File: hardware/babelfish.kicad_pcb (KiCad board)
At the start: 4 copper layers, 56 x 45.2 mm, 97 parts, among them J1 Shifter Power, J2 SWD, J3 DE9 Female, J4 USB_A, Q1 BSS138, SW1 TS342A2P-WZ, SW2 TS342A2P-WZ, SW3 SK12D07VG5_C3020419, U1 RP2040, U10 74HC4052PW,118, U11 MAX3232IDR, U12 AP2191WG-7, U2 TPS2113ADRBR, U3 GT-USB-7010ASV, U4 W25Q128JVS, U5 TPMCP1703T-5002E_CB, U6 TPMCP1703T-3302E_CB, U7 74HC4052PW,118, U8 74HC4052PW,118, U9 74HC4052PW,118, X1 X322512MSB4SI

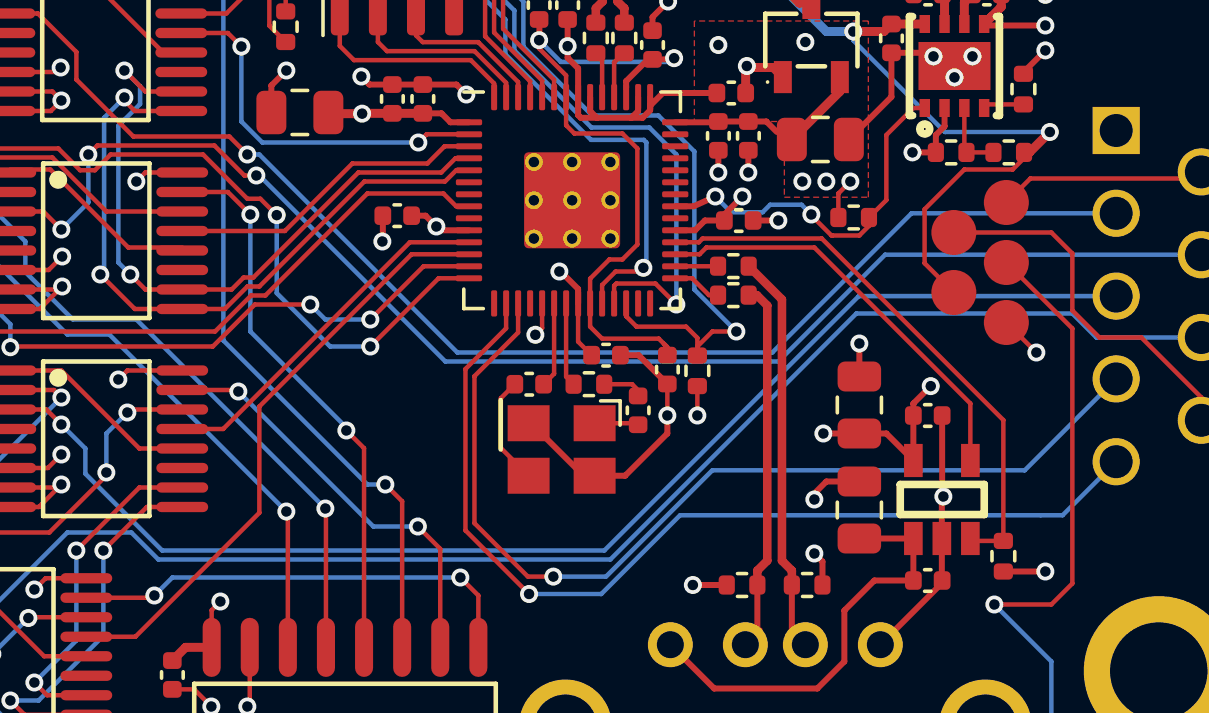
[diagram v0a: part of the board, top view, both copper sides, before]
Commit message: Er, forgot to wire CH_B_S0/1
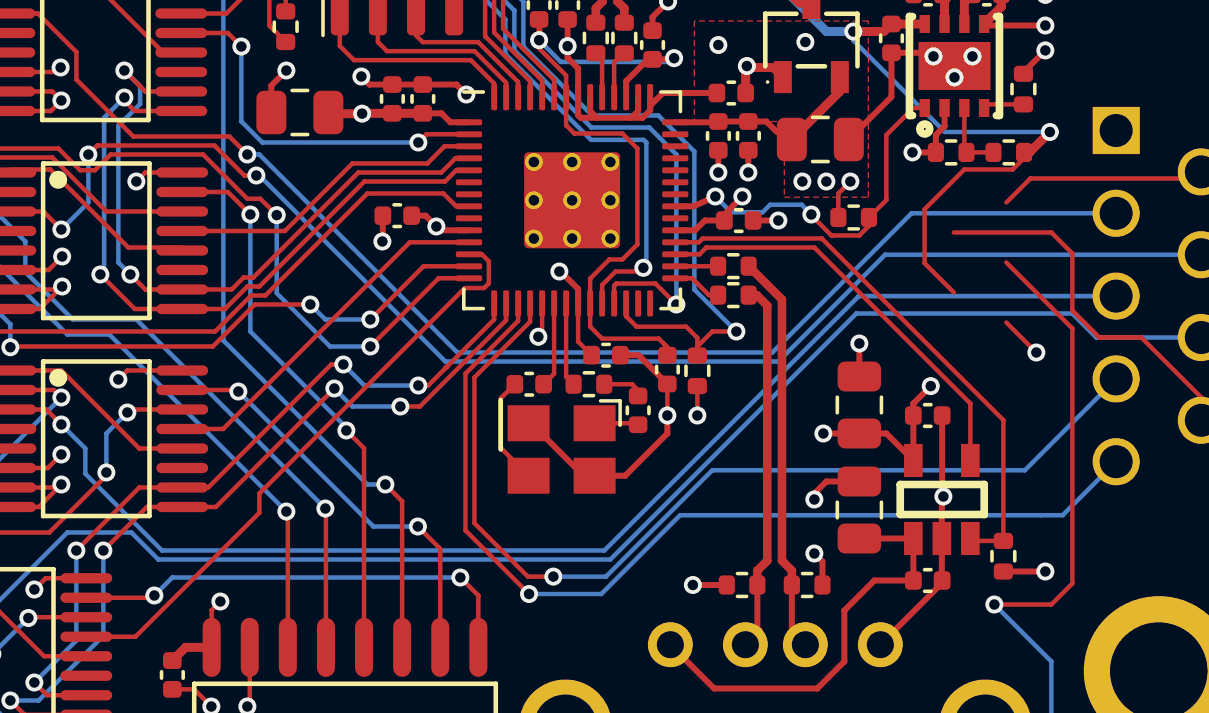
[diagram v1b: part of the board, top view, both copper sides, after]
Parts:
- removed ? (x5): , 
- D3: value Blue -> Red
- R15, R16, R17: value 68 -> 1k
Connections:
- J3 pad 4: /GPIO14 -> /GPIO15
- J3 pad 5: /GPIO13 -> /GPIO14
- U1 pad 15: /GPIO12 -> /CH_B_S0
- U1 pad 16: /GPIO13 -> /CH_B_S1
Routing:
- net /GPIO15: track 0.00 -> 33.0 mm, vias 0 -> 1
- net /GPIO13: track 32.5 -> 0.00 mm, vias 1 -> 0
- net /CH_B_S1: track 12.8 -> 27.2 mm, vias 2 -> 4
- net /CH_B_S0: track 11.3 -> 25.2 mm, vias 2 -> 4

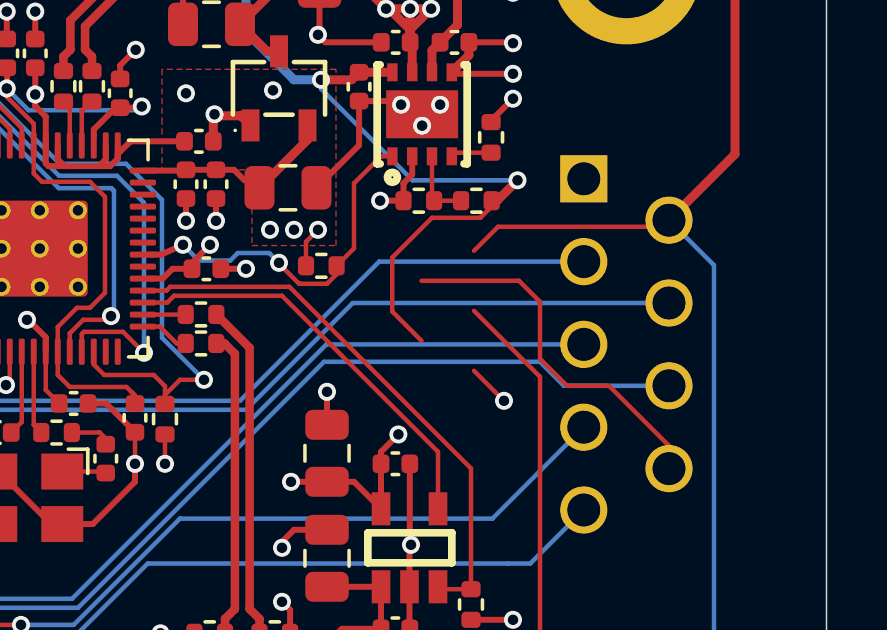
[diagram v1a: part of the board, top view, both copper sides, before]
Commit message: hw: Add back test points to schematic, fix db9 GND
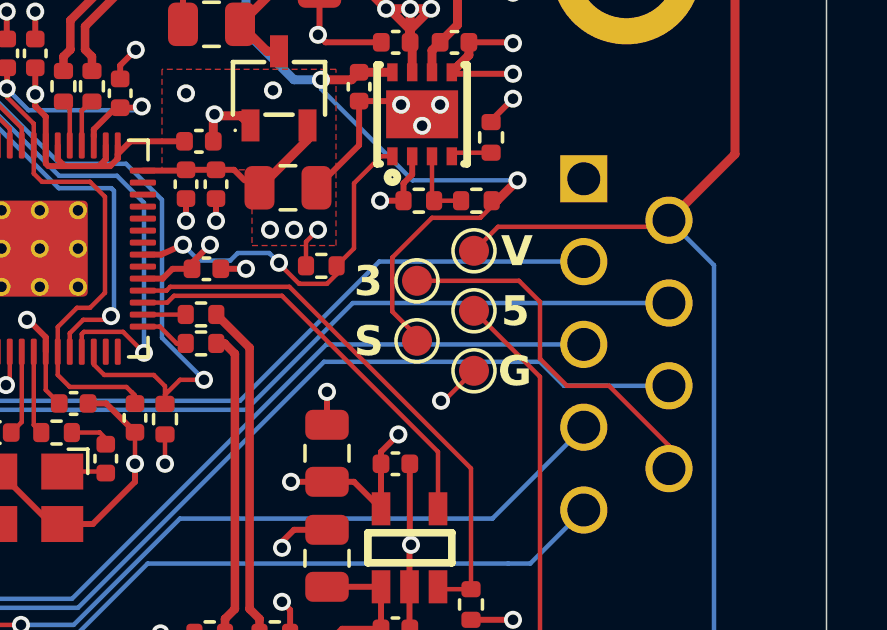
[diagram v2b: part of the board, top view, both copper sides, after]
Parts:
- added TP1: TestPoint, TestPoint:TestPoint_Pad_D1.0mm, F.Cu at (124.6, 90.0)
- added TP2: TestPoint, TestPoint:TestPoint_Pad_D1.0mm, F.Cu at (126.5, 89.0)
- added TP3: TestPoint, TestPoint:TestPoint_Pad_D1.0mm, F.Cu at (124.6, 92.0)
- added TP4: TestPoint, TestPoint:TestPoint_Pad_D1.0mm, F.Cu at (126.5, 91.0)
- added TP5: TestPoint, TestPoint:TestPoint_Pad_D1.0mm, F.Cu at (126.5, 93.0)
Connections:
- net /U1_RX_A renamed /GPIO5
- net /U1_TX_A renamed /GPIO4
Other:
- board text added: "3"
- board text added: "5"
- board text added: "G"
- board text added: "S"
- board text added: "V"

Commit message: hw v0.3
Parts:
- moved C1 80.2 mm to (50.1, 47.7)
- moved C11 80.2 mm to (49.2, 49.0)
- moved C19 80.2 mm to (62.4, 31.2)
- moved C23 80.2 mm to (33.6, 59.9)
- moved C24 80.2 mm to (35.4, 64.1)
- moved D3 80.2 mm to (22.6, 47.5)
- moved R17 80.2 mm to (22.6, 44.4)
- moved R24 80.2 mm to (22.1, 60.0)
- moved R25 80.2 mm to (22.6, 54.7)
- moved R28 80.2 mm to (61.4, 53.9)
- moved R5 80.2 mm to (47.7, 31.5)
- moved U7 80.2 mm to (31.1, 36.8)
- moved C10 80.2 mm to (52.5, 42.7)
- moved C12 80.2 mm to (45.5, 48.2)
- moved C13 80.2 mm to (49.7, 36.9)
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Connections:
- J3 pad 10: (no net) -> GND
- J3 pad 11: (no net) -> GND
- U1 pad 36: unconnected-(U1-GPIO24-Pad36) -> /GPIO24
- U1 pad 37: unconnected-(U1-GPIO25-Pad37) -> /GPIO25
- U10 pad 11: unconnected-(U10-1Y3-Pad11) -> GND
- U7 pad 4: unconnected-(U7-2Y3-Pad4) -> GND
- U8 pad 11: unconnected-(U8-1Y3-Pad11) -> GND
- U9 pad 4: unconnected-(U9-2Y3-Pad4) -> GND
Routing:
- net GND: track 130.5 -> 143.3 mm
- net /CH_A_S1: track 23.1 -> 23.8 mm

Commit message: WIP new power
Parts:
- removed C19, C20: 10u, Capacitor_SMD:C_0805_2012Metric
- removed J1: Shifter Power, Connector_PinHeader_2.54mm:PinHeader_1x03_P2.54mm_Vertical
- removed SW3: SK12D07VG5_C3020419, lcsc:SW-TH_SHOU_SK12D07VG5
- removed U10, U9: 74HC4052PW,118, lcsc:TSSOP-16_L5.0-W4.4-P0.65-LS6.4-BL
- removed U5: TPMCP1703T-5002E_CB, lcsc:SOT-23-3_L2.9-W1.6-P1.90-LS2.8-BR
- added C36: 100n, Capacitor_SMD:C_01005_0402Metric, F.Cu at (87.4, 47.8)
- added C37: 10u, Capacitor_SMD:C_0805_2012Metric, F.Cu at (76.0, 47.5)
- added C38: 100n, Capacitor_SMD:C_0402_1005Metric, F.Cu at (77.8, 46.6)
- added C39: 33n, Capacitor_SMD:C_01005_0402Metric, F.Cu at (86.2, 46.8)
- added C40: 47p, Capacitor_SMD:C_0402_1005Metric, F.Cu at (82.3, 44.9)
- added C41: 22u, Capacitor_SMD:C_0805_2012Metric, F.Cu at (87.5, 44.3)
- added DIP1: KF1001-08P-R0-GL-DFT-01B, lcsc:SW-TH_16P-L21.9-W9.9-P2.54-LS7.6, F.Cu at (99.1, 22.9)
- added DIP2: DSWB04LHGET, lcsc:SW-TH_DSWB04LHGET, F.Cu at (95.7, 33.8)
- added L36: 2.7uH, Inductor_SMD:L_12x12mm_H6mm, F.Cu at (118.2, 59.0)
- added R36: 52k3, Resistor_SMD:R_0402_1005Metric, F.Cu at (82.6, 42.8)
- added R37: 15k, Resistor_SMD:R_0402_1005Metric, F.Cu at (77.6, 43.2)
- added R38: 10k, Resistor_SMD:R_0402_1005Metric, F.Cu at (84.2, 46.2)
- added U36: TPS62933, Package_TO_SOT_SMD:SOT-583-8, F.Cu at (79.7, 45.6)
- moved TP2 53.3 mm to (38.1, 90.0)
- moved TP4 53.3 mm to (38.1, 92.0)
- moved TP5 53.3 mm to (38.1, 94.0)
- moved TP1 53.3 mm to (36.2, 91.0)
- moved TP3 53.3 mm to (36.2, 93.0)
- moved J3 44.8 mm to (95.1, 79.7)
- moved C21 7.43 mm to (59.5, 37.5), turned to -90 degrees
- moved C18 5.88 mm to (66.7, 35.2)
- moved R9 5.88 mm to (67.9, 38.3)
- moved C15 5.88 mm to (63.5, 36.6)
- moved C17 5.88 mm to (64.7, 35.2)
- moved R6 5.88 mm to (67.4, 40.4)
- moved U2 5.88 mm to (65.6, 37.5)
- moved R8 5.88 mm to (65.5, 40.4)
- moved U6 0.87 mm to (55.8, 37.0), turned to 180 degrees
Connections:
- U7 pad 1: /TX_A_Y0_THRU -> /RX_A_CONN
- U7 pad 12: /TX_A_Y0_THRU -> /TX_A_CONN
- U7 pad 2: /TX_A_2Y2 -> /RX_A_1Y2
- U7 pad 3: /TX_A_CONN -> /RX_A
- U7 pad 4: GND -> unconnected-(U7-2Y3-Pad4)
- U7 pad 5: /TX_A_2Y1 -> /RX_A_1Y1
- U8 pad 1: /RX_A_Y0_THRU -> /RX_B_CONN
- U8 pad 10: /CH_A_S0 -> /CH_B_S0
- U8 pad 11: GND -> unconnected-(U8-1Y3-Pad11)
- U8 pad 12: /RX_A_Y0_THRU -> /TX_B_CONN
- U8 pad 13: /RX_A -> /TX_B
- U8 pad 14: /RX_A_1Y1 -> /TX_B_1Y1
- U8 pad 15: /RX_A_1Y2 -> /TX_B_1Y2
- U8 pad 2: /RX_A_2Y2 -> /RX_B_1Y2
- U8 pad 3: /RX_A_CONN -> /RX_B
- U8 pad 5: /RX_A_2Y1 -> /RX_B_1Y1
- U8 pad 9: /CH_A_S1 -> /CH_B_S1
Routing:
- net /VCC_IN: track 98.2 -> 0.00 mm
- net /5V0: track 75.5 -> 7.12 mm, vias 6 -> 2
- net /RX_B_CONN: track 48.6 -> 0.00 mm, vias 1 -> 0
- net /RX_A_CONN: track 46.5 -> 0.00 mm, vias 3 -> 0
- net /TX_A_CONN: track 44.3 -> 0.00 mm, vias 1 -> 0
- net /TX_B_CONN: track 42.8 -> 0.00 mm, vias 1 -> 0
- net GND: track 143.3 -> 105.6 mm, vias 50 -> 40
- net /TX_B_2Y2: track 35.0 -> 0.00 mm, vias 2 -> 0
- net /GPIO15: track 33.0 -> 0.00 mm, vias 1 -> 0
- net /GPIO14: track 32.7 -> 0.00 mm, vias 1 -> 0
- net /TX_A_2Y2: track 28.8 -> 0.00 mm, vias 2 -> 0
- net /CH_B_S1: track 27.2 -> 0.00 mm, vias 4 -> 0
- net /RX_B_2Y2: track 26.8 -> 0.00 mm, vias 2 -> 0
- net /CH_B_S0: track 25.2 -> 0.00 mm, vias 4 -> 0
- net /CH_A_S1: track 23.8 -> 0.00 mm, vias 2 -> 0
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- added copper zone on F.Cu, net /VCC_IN_SW
- added copper zone on F.Cu, net GND
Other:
- board size 56 x 45.2 mm -> 76 x 45.2 mm

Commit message: WIP -- pre-shift-up
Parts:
- L36: footprint Inductor_SMD:L_12x12mm_H6mm -> lcsc:IND-SMD_L6.0-W6.0_FNR60XXS
- moved L36 47.1 mm to (72.6, 47.1), turned to 90 degrees
- moved DIP1 44.5 mm to (56.5, 9.91)
- moved J3 41.9 mm to (86.1, 38.8)
- moved DIP2 28.6 mm to (85.2, 60.4), turned to 180 degrees
- moved C36 15.7 mm to (72.3, 52.0), turned to 0 degrees
- moved R36 14.9 mm to (72.7, 54.0), turned to 90 degrees
- moved C39 14.7 mm to (72.8, 52.7), turned to 0 degrees
- moved C40 13.9 mm to (71.7, 54.0), turned to 90 degrees
- moved R38 13.1 mm to (73.7, 54.0), turned to -90 degrees
- moved C41 11.8 mm to (76.0, 41.7)
- moved R37 11.3 mm to (76.7, 54.5), turned to 180 degrees
- moved U36 8.07 mm to (75.6, 52.5), turned to 180 degrees
- moved C38 4.94 mm to (77.5, 51.6), turned to 90 degrees
- moved C37 4.60 mm to (79.4, 50.6), turned to 90 degrees
- moved R6 4.52 mm to (63.0, 39.6), turned to 90 degrees
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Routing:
- net /VCC_IN: track 0.00 -> 38.8 mm
- net /VCC_5V: track 1.11 -> 23.5 mm, vias 0 -> 2
- net /5V0: track 7.12 -> 24.8 mm
- net /VCC_IN_SW: track 0.00 -> 12.6 mm
- net VBUS: track 25.6 -> 35.4 mm, vias 2 -> 4
- net GND: track 105.6 -> 109.5 mm, vias 40 -> 95
- net /VSHIFT: track 43.9 -> 46.4 mm
- net Net-(U36-BST): track 0.00 -> 2.37 mm
- net Net-(U36-RT): track 0.00 -> 1.93 mm
- net Net-(U36-SS): track 0.00 -> 1.85 mm
- net /STAT_5V0: track 7.00 -> 5.34 mm
- net Net-(U36-SW): track 0.00 -> 0.85 mm
- net +3V3: track 56.8 -> 56.4 mm, vias 19 -> 18
- net (no net): vias 0 -> 1
- added copper zone on F.Cu, net /VCC_5V
- added copper zone on F.Cu, net Net-(U36-FB)
- added copper zone on F.Cu, net Net-(U36-SW)

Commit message: WIP dip switches
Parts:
- moved DIP1 88.4 mm to (93.5, 90.2)
- moved R37 29.5 mm to (72.0, 25.4), turned to 0 degrees
- moved C40 28.6 mm to (77.0, 25.9), turned to -90 degrees
- moved R36 28.3 mm to (76.0, 25.9), turned to -90 degrees
- moved R38 28.2 mm to (75.0, 25.9), turned to 90 degrees
- moved C39 25.7 mm to (76.0, 27.2), turned to 180 degrees
- moved U36 25.3 mm to (73.1, 27.4), turned to 0 degrees
- moved C36 24.5 mm to (76.4, 27.9), turned to 180 degrees
- moved H2 24.5 mm to (94.2, 64.4)
- moved C38 24.1 mm to (71.2, 28.3), turned to -90 degrees
- moved C37 23.7 mm to (69.3, 29.2), turned to -90 degrees
- moved R8 18.2 mm to (80.8, 41.5), turned to -90 degrees
- moved R6 17.8 mm to (80.8, 39.6), turned to -90 degrees
- moved C29 15.9 mm to (72.3, 54.0), turned to 0 degrees
- moved C31 14.8 mm to (70.9, 45.4), turned to 0 degrees
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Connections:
- DIP2 pad 1: /VCC_IN -> /VSHIFT
- DIP2 pad 2: /VCC_IN -> /VSHIFT
- DIP2 pad 3: /VCC_IN -> /VCC_5V
- DIP2 pad 4: /5V0 -> /VCC_IN_SW
- DIP2 pad 5: /VCC_IN_SW -> /5V0
- DIP2 pad 6: /VCC_5V -> /VCC_IN
- DIP2 pad 7: /VSHIFT -> /VCC_IN
- DIP2 pad 8: /VSHIFT -> /VCC_IN
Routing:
- net /TX_A_1Y2: track 26.9 -> 13.9 mm, vias 2 -> 1
- net /USB2_FLG: track 18.7 -> 6.76 mm
- net /5V0: track 24.8 -> 13.2 mm, vias 2 -> 8
- net /USB2_D+: track 13.4 -> 4.36 mm
- net /USB2_D-: track 13.1 -> 5.11 mm
- net /VCC_IN_SW: track 12.6 -> 4.93 mm
- net /USB2_EN: track 14.0 -> 6.63 mm
- net /VCC_IN: track 38.8 -> 44.3 mm
- net /VCC_5V: track 23.5 -> 18.9 mm
- net GND: track 109.5 -> 113.8 mm, vias 95 -> 96
- net /VBUS_OUT: track 14.4 -> 18.4 mm
- net VBUS: track 35.4 -> 36.5 mm
- net +3V3: track 56.4 -> 55.8 mm
- added copper zone on F.Cu, net /5V0

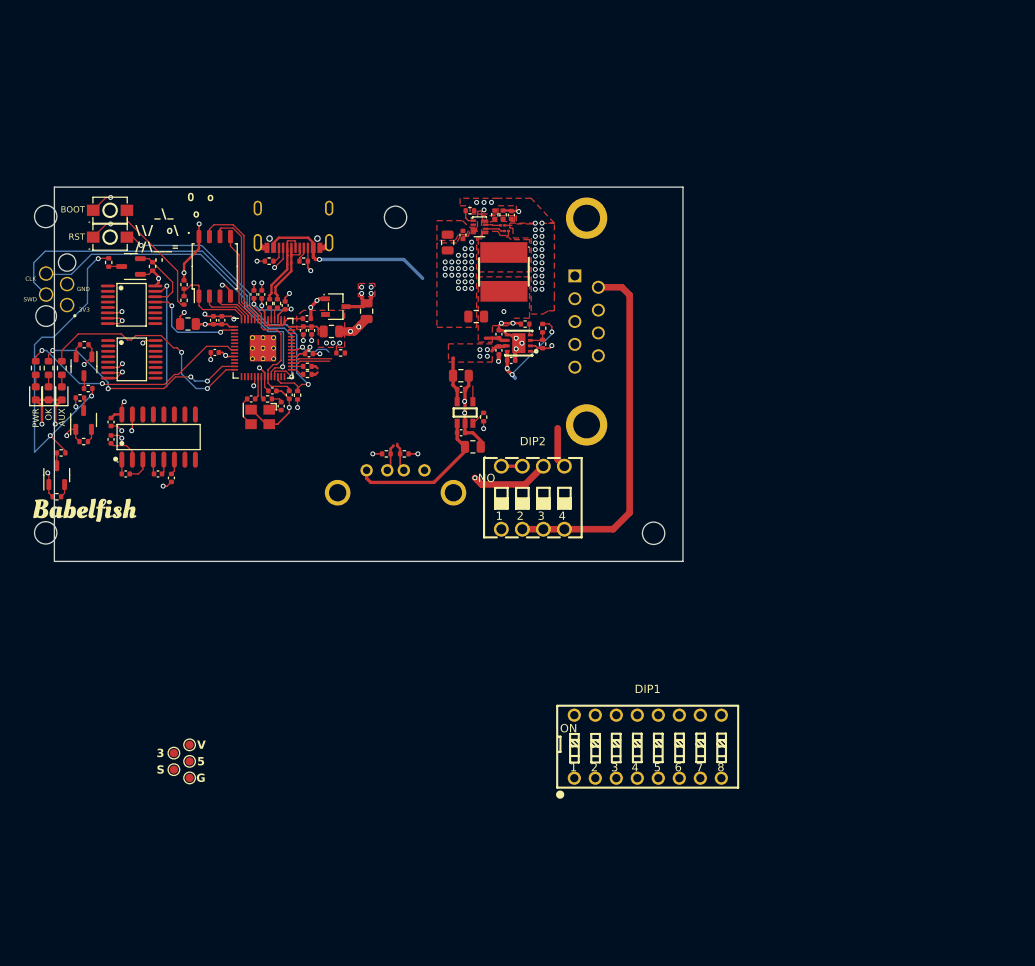
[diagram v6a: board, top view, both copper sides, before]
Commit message: Finished complex DC-DC layout, pre-deletion
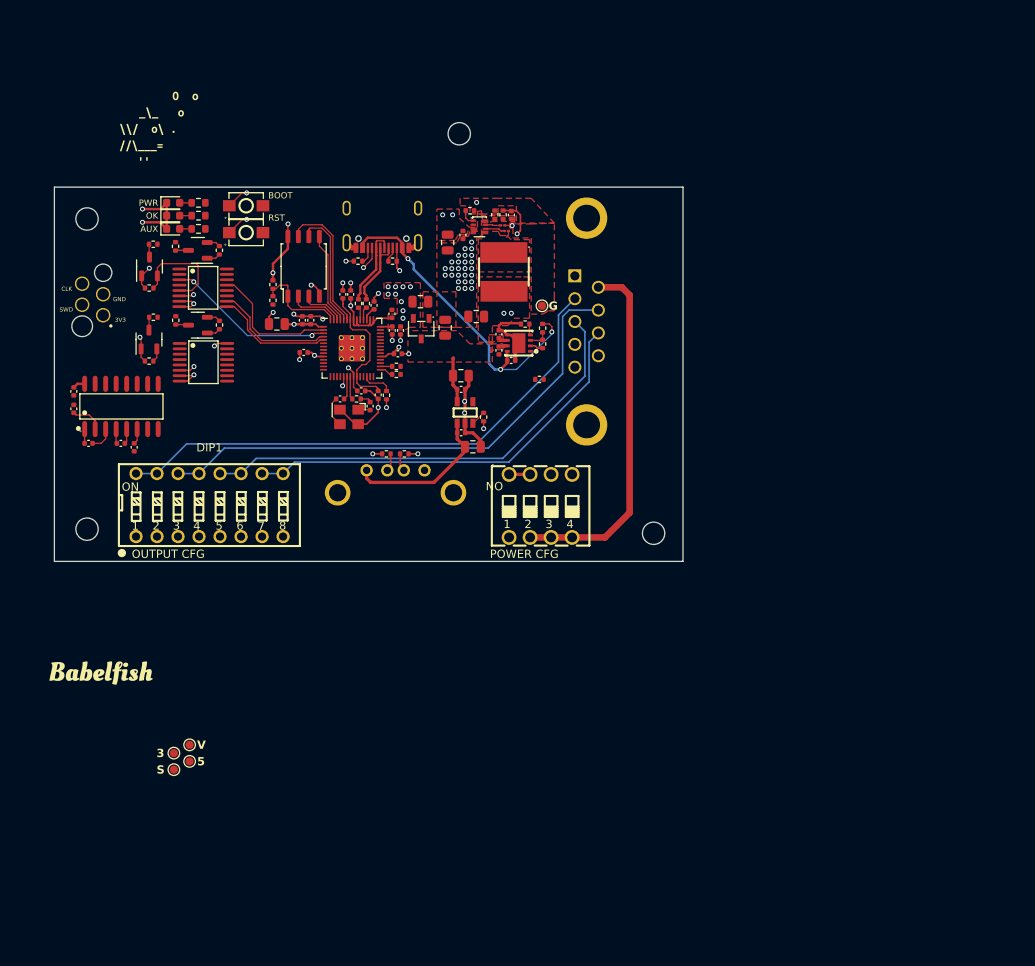
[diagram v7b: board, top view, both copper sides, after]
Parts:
- moved TP5 71.2 mm to (80.7, 36.9)
- moved DIP1 60.5 mm to (40.5, 61.0)
- moved D1 28.4 mm to (36.1, 24.4), turned to 0 degrees
- moved R15 28.0 mm to (39.2, 24.4), turned to 180 degrees
- moved D2 26.2 mm to (36.1, 26.0), turned to 0 degrees
- moved R16 25.8 mm to (39.2, 26.0), turned to 180 degrees
- moved R2 24.2 mm to (80.4, 45.8)
- moved D3 24.0 mm to (36.1, 27.6), turned to 0 degrees
- moved R17 23.6 mm to (39.2, 27.6), turned to 180 degrees
- moved R22 21.6 mm to (41.7, 39.2), turned to 90 degrees
- moved Q4 19.8 mm to (33.2, 41.0)
- moved R24 19.8 mm to (33.2, 43.6)
- moved R25 19.8 mm to (33.7, 38.3)
- moved kibuzzard-644F3679 19.8 mm to (27.4, 81.3)
- moved R19 19.1 mm to (33.7, 29.5)
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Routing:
- net /TX_A_CONN: track 0.00 -> 65.1 mm
- net /RX_A_CONN: track 0.00 -> 63.1 mm
- net /TX_B_CONN: track 0.00 -> 56.1 mm
- net /RX_B_CONN: track 0.00 -> 50.5 mm
- net /SWD: track 49.2 -> 0.00 mm, vias 1 -> 0
- net /VSHIFT: track 46.4 -> 2.54 mm, vias 4 -> 0
- net /SWCLK: track 40.8 -> 0.00 mm, vias 1 -> 0
- net /VCC_IN_SW: track 4.93 -> 43.0 mm, vias 0 -> 2
- net /RUN: track 38.1 -> 3.69 mm, vias 2 -> 0
- net GND: track 113.8 -> 83.2 mm, vias 96 -> 56
- net /LED_PWR: track 28.7 -> 0.00 mm, vias 2 -> 0
- net /LED_AUX: track 28.7 -> 0.00 mm, vias 2 -> 0
- net /LED_P_OK: track 27.4 -> 0.00 mm, vias 4 -> 0
- net /VCC_5V: track 18.9 -> 43.3 mm, vias 2 -> 3
- net /RX_A: track 0.00 -> 20.3 mm, vias 0 -> 2
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- removed copper zone on In2.Cu, net /5V0
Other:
- board text added: "OUTPUT CFG"
- board text added: "POWER CFG"
